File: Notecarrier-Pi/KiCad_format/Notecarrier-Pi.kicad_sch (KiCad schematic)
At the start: 47 parts, among them J1 2223, J3 MDT420E01001, J4 10118192-0002LF, J5 GROVE, J5 NanoSIM - SF72S006VBAR2500

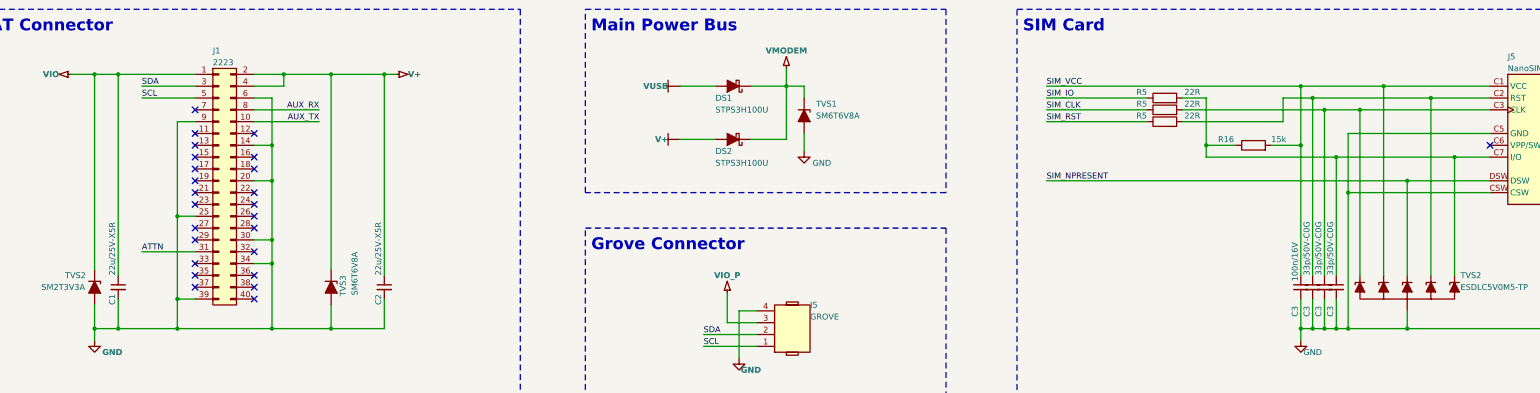
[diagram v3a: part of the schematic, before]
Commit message: Complete validation of Notecarrier-Pi port.
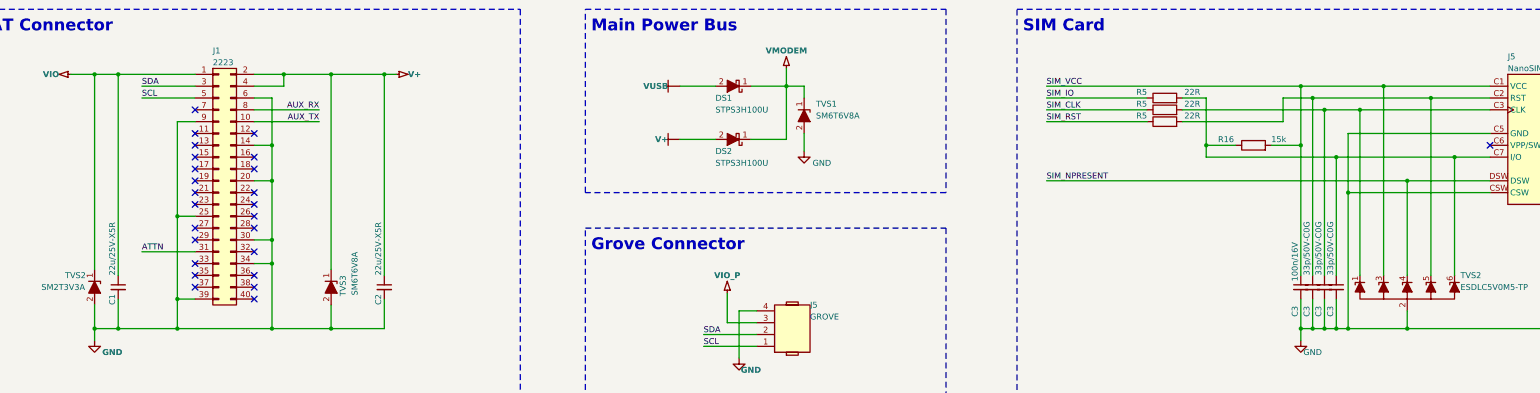
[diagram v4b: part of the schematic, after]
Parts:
- H1, H2, H3, H4: footprint blues-kicad-lib:FORO-0270-U -> blues-kicad-lib:FORO-0270-U_smaller-clearance
- J4: footprint blues-kicad-lib:J-5-0065-FOS-MICROUSB10118192 -> blues-kicad-lib:J-5-0065-FOS-USB10118192-NOF; Distributor (none) -> FAE; MPN 10118192-0001LF -> 10118192-0002LF
- TVS2: footprint blues-kicad-lib:SOT563 -> blues-kicad-lib:SOT666_NO-SILK
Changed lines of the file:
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@@
     )
   )
-  (symbol (lib_id "blues-kicad-lib:SM6T6V8A") (at 203.2 41.91 270) (unit 1)
+  (symbol (lib_name "SM6T6V8A_1") (lib_id "blues-kicad-lib:SM6T6V8A") (at 203.2 41.91 270) (unit 1)
     (in_bom yes) (on_board yes) (dnp no)
     (property "Reference" "TVS1" (at 205.74 39.37 90)
@@
     )
     (property "Distributor" "FAE" (at 203.2 41.91 0)
+      (effects (font (size 1.27 1.27)) hide)
+    )
+    (property "Critical" "" (at 203.2 41.91 0)
+      (effects (font (size 1.27 1.27)) hide)
+    )
+    (property "Manufacturer" "" (at 203.2 41.91 0)
+      (effects (font (size 1.27 1.27)) hide)
+    )
+    (property "Order Code" "" (at 203.2 41.91 0)
+      (effects (font (size 1.27 1.27)) hide)
+    )
+    (property "Part Number" "" (at 203.2 41.91 0)
+      (effects (font (size 1.27 1.27)) hide)
+    )
+    (property "Supplier" "" (at 203.2 41.91 0)
       (effects (font (size 1.27 1.27)) hide)
     )
@@
       (effects (font (size 1.27 1.27)) hide)
     )
+    (property "Critical" "" (at 187.96 46.99 0)
+      (effects (font (size 1.27 1.27)) hide)
+    )
+    (property "Manufacturer" "" (at 187.96 46.99 0)
+      (effects (font (size 1.27 1.27)) hide)
+    )
+    (property "Order Code" "" (at 187.96 46.99 0)
+      (effects (font (size 1.27 1.27)) hide)
+    )
+    (property "Part Number" "" (at 187.96 46.99 0)
+      (effects (font (size 1.27 1.27)) hide)
+    )
+    (property "Supplier" "" (at 187.96 46.99 0)
+      (effects (font (size 1.27 1.27)) hide)
+    )
     (pin "1")
     (pin "2")
@@
       (effects (font (size 1.27 1.27)) (justify left))
     )
-    (property "Footprint" "blues-kicad-lib:SOT563" (at 332.74 91.44 0)
+    (property "Footprint" "blues-kicad-lib:SOT666_NO-SILK" (at 332.74 91.44 0)
       (effects (font (size 1.27 1.27)) hide)
     )
@@
       (effects (font (size 1.27 1.27)) hide)
     )
+    (property "Critical" "" (at 101.6 78.74 0)
+      (effects (font (size 1.27 1.27)) hide)
+    )
+    (property "Manufacturer" "" (at 101.6 78.74 0)
+      (effects (font (size 1.27 1.27)) hide)
+    )
+    (property "Order Code" "" (at 101.6 78.74 0)
+      (effects (font (size 1.27 1.27)) hide)
+    )
+    (property "Part Number" "" (at 101.6 78.74 0)
+      (effects (font (size 1.27 1.27)) hide)
+    )
+    (property "Supplier" "" (at 101.6 78.74 0)
+      (effects (font (size 1.27 1.27)) hide)
+    )
     (pin "1")
     (pin "2")
@@
       (effects (font (size 1.27 1.27)) (justify right))
     )
-    (property "Footprint" "blues-kicad-lib:J-5-0065-FOS-MICROUSB10118192" (at 289.56 140.97 0)
+    (property "Footprint" "blues-kicad-lib:J-5-0065-FOS-USB10118192-NOF" (at 289.56 140.97 0)
       (effects (font (size 1.27 1.27)) hide)
     )
@@
       (effects (font (size 1.27 1.27)) hide)
     )
-    (property "Description" "CONN. USB F/90° TYPE MICRO-B C.S. 10118192-0001LF FCI SMT" (at 293.37 139.7 0)
+    (property "Description" "CONN. USB F/90° TYPE MICRO-B C.S. 10118192-0002LF FCI SMT" (at 293.37 139.7 0)
       (effects (font (size 1.27 1.27)) hide)
     )
@@
       (effects (font (size 1.27 1.27)) hide)
     )
-    (property "MPN" "10118192-0001LF" (at 293.37 139.7 0)
+    (property "MPN" "10118192-0002LF" (at 293.37 139.7 0)
       (effects (font (size 1.27 1.27)) hide)
     )
@@
     )
     (property "Note" "Full SMD, no FLANGE" (at 293.37 139.7 0)
+      (effects (font (size 1.27 1.27)) hide)
+    )
+    (property "Critical" "" (at 293.37 139.7 0)
+      (effects (font (size 1.27 1.27)) hide)
+    )
+    (property "Manufacturer" "" (at 293.37 139.7 0)
+      (effects (font (size 1.27 1.27)) hide)
+    )
+    (property "Order Code" "" (at 293.37 139.7 0)
+      (effects (font (size 1.27 1.27)) hide)
+    )
+    (property "Part Number" "" (at 293.37 139.7 0)
+      (effects (font (size 1.27 1.27)) hide)
+    )
+    (property "Supplier" "" (at 293.37 139.7 0)
+      (effects (font (size 1.27 1.27)) hide)
+    )
+    (property "Distributor" "FAE" (at 293.37 139.7 0)
       (effects (font (size 1.27 1.27)) hide)
     )
@@
     )
   )
-  (symbol (lib_id "blues-kicad-lib:SM6T6V8A") (at 50.8 78.74 270) (unit 1)
+  (symbol (lib_name "SM6T6V8A_2") (lib_id "blues-kicad-lib:SM6T6V8A") (at 50.8 78.74 270) (unit 1)
     (in_bom yes) (on_board yes) (dnp no)
     (property "Reference" "TVS2" (at 44.45 76.2 90)
@@
       (effects (font (size 1.27 1.27)) (justify left) hide)
     )
-    (property "Footprint" "blues-kicad-lib:FORO-0270-U" (at 242.57 267.97 0)
+    (property "Footprint" "blues-kicad-lib:FORO-0270-U_smaller-clearance" (at 242.57 267.97 0)
       (effects (font (size 1.27 1.27)) hide)
     )
@@
     )
   )
-  (symbol (lib_id "Device:D_Schottky_Filled") (at 187.96 35.56 180) (unit 1)
+  (symbol (lib_name "D_Schottky_Filled_1") (lib_id "Device:D_Schottky_Filled") (at 187.96 35.56 180) (unit 1)
     (in_bom yes) (on_board yes) (dnp no)
     (property "Reference" "DS1" (at 184.15 38.1 0)
@@
       (effects (font (size 1.27 1.27)) hide)
     )
+    (property "Critical" "" (at 187.96 35.56 0)
+      (effects (font (size 1.27 1.27)) hide)
+    )
+    (property "Manufacturer" "" (at 187.96 35.56 0)
+      (effects (font (size 1.27 1.27)) hide)
+    )
+    (property "Order Code" "" (at 187.96 35.56 0)
+      (effects (font (size 1.27 1.27)) hide)
+    )
+    (property "Part Number" "" (at 187.96 35.56 0)
+      (effects (font (size 1.27 1.27)) hide)
+    )
+    (property "Supplier" "" (at 187.96 35.56 0)
+      (effects (font (size 1.27 1.27)) hide)
+    )
     (pin "1")
     (pin "2")
@@
       (effects (font (size 1.27 1.27)) (justify left) hide)
     )
-    (property "Footprint" "blues-kicad-lib:FORO-0270-U" (at 248.92 267.97 0)
+    (property "Footprint" "blues-kicad-lib:FORO-0270-U_smaller-clearance" (at 248.92 267.97 0)
       (effects (font (size 1.27 1.27)) hide)
     )
@@
       (effects (font (size 1.27 1.27)) (justify left) hide)
     )
-    (property "Footprint" "blues-kicad-lib:FORO-0270-U" (at 242.57 261.62 0)
+    (property "Footprint" "blues-kicad-lib:FORO-0270-U_smaller-clearance" (at 242.57 261.62 0)
       (effects (font (size 1.27 1.27)) hide)
     )
@@
       (effects (font (size 1.27 1.27)) (justify left) hide)
     )
-    (property "Footprint" "blues-kicad-lib:FORO-0270-U" (at 248.92 261.62 0)
-      (effects (font (size 1.27 1.27)) hide)
-    )
+    (property "Footprint" "blues-kicad-lib:FORO-0270-U_smaller-clearance" (at 248.92 261.62 0)
+      (effects (font (size 1.27 1.27)) hide)
+    )
